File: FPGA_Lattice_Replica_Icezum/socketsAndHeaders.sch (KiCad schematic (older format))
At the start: 38 parts, among them J10 1x8_male_pin_Header_2.54mm, J11 1x6_female_pin_Header_2.54mm, J12 1x6_female_pin_Header_2.54mm, J13 1x6_female_pin_Header_2.54mm, J14 1x6_female_pin_Header_2.54mm, J2 1x6_female_pin_Header_2.54mm, J3 1x6_female_pin_Header_2.54mm, J4 1x10_female_pin_Header_2.54mm, J5 1x8_male_pin_Header_2.54mm, J6 1x6_female_pin_Header_2.54mm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

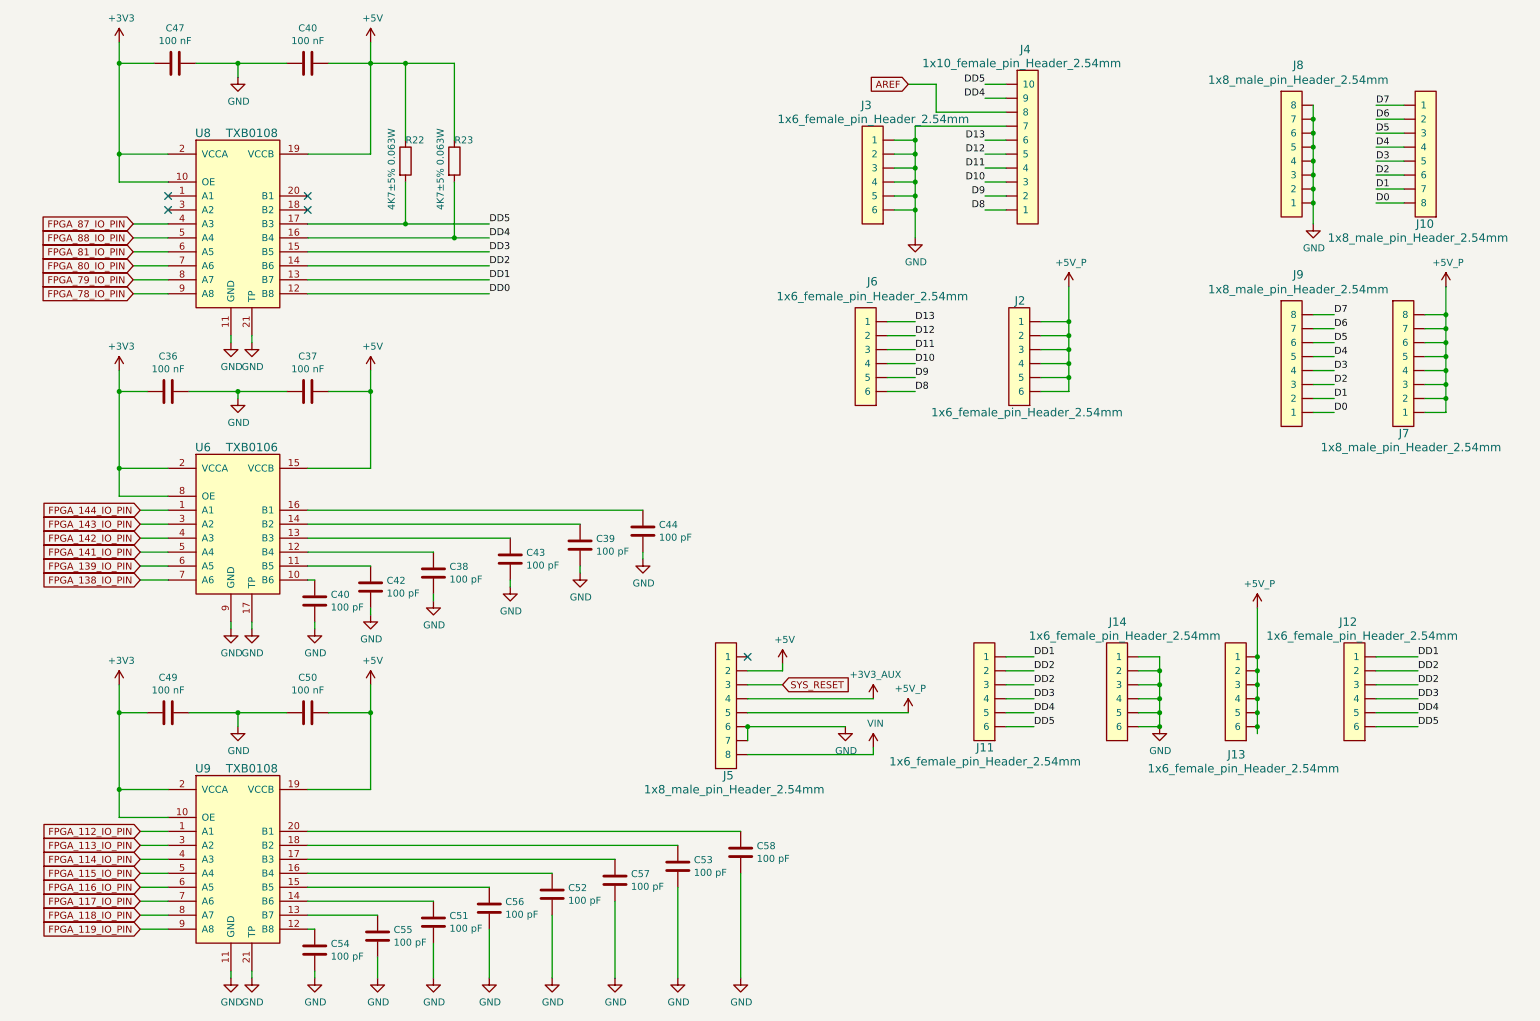
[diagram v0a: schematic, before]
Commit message: se ejecuto y se corrigio electrical rules check
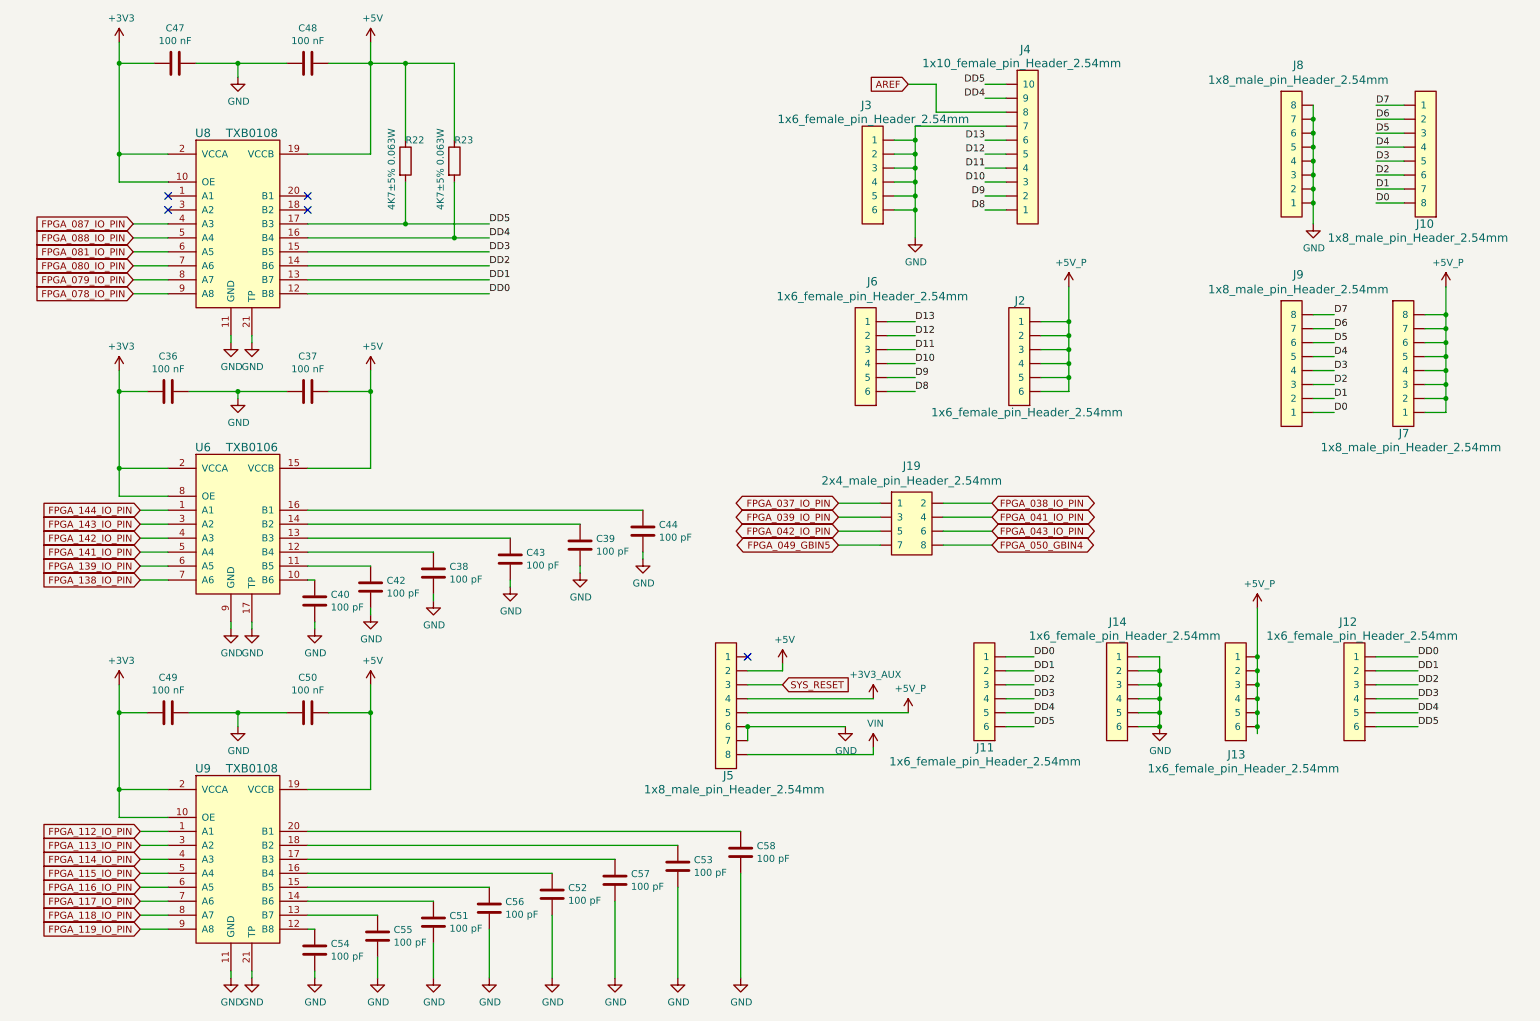
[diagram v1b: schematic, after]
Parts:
- added J19: 2x4_male_pin_Header_2.54mm, symbol icezum:2x4_male_pin_Header_2.54mm
- renumbered C40 to C48
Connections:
- net DD0: now also J11.1, J12.1
- net DD1: now also J11.2, J12.2; no longer J11.1, J12.1
- net DD2: no longer J11.2, J12.2
- net FPGA_78_IO_PIN renamed FPGA_078_IO_PIN
- net FPGA_79_IO_PIN renamed FPGA_079_IO_PIN
- net FPGA_80_IO_PIN renamed FPGA_080_IO_PIN
- net FPGA_81_IO_PIN renamed FPGA_081_IO_PIN
- net FPGA_87_IO_PIN renamed FPGA_087_IO_PIN
- net FPGA_88_IO_PIN renamed FPGA_088_IO_PIN
- new net FPGA_037_IO_PIN: J19.1
- new net FPGA_038_IO_PIN: J19.2
- new net FPGA_039_IO_PIN: J19.3
- new net FPGA_041_IO_PIN: J19.4
- new net FPGA_042_IO_PIN: J19.5
- new net FPGA_043_IO_PIN: J19.6
- new net FPGA_049_GBIN5: J19.7
- new net FPGA_050_GBIN4: J19.8

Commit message: se comenzo asignacion de footprints
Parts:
- C38, C39, C40, C42, C43, C44, C51, C52: footprint (none) -> footprints:C_0402
- C49: footprint (none) -> footprints:C_0603
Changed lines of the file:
@@
 F 0 "U8" H 1850 1650 60  0000 C CNN
 F 1 "TXB0108" H 2200 1650 60  0000 C CNN
-F 2 "" H 2050 1600 60  0000 C CNN
+F 2 "" H 2050 1600 60  0001 C CNN
 F 3 "" H 2050 1600 60  0000 C CNN
 	1    1600 1500
@@
 F 0 "U9" H 1850 6200 60  0000 C CNN
 F 1 "TXB0108" H 2200 6200 60  0000 C CNN
-F 2 "" H 2050 6150 60  0000 C CNN
+F 2 "" H 2050 6150 60  0001 C CNN
 F 3 "" H 2050 6150 60  0000 C CNN
 	1    1600 6050
@@
 F 0 "U6" H 1850 3900 60  0000 C CNN
 F 1 "TXB0106" H 2200 3900 60  0000 C CNN
-F 2 "" H 2050 3850 60  0000 C CNN
+F 2 "" H 2050 3850 60  0001 C CNN
 F 3 "" H 2050 3850 60  0000 C CNN
 	1    1600 3750
@@
 F 0 "C49" V 1348 5500 50  0000 C CNN
 F 1 "100 nF" V 1439 5500 50  0000 C CNN
-F 2 "" H 1638 5350 50  0001 C CNN
+F 2 "footprints:C_0603" H 1638 5350 50  0001 C CNN
 F 3 "~" H 1600 5500 50  0001 C CNN
 	1    1600 5500
@@
 F 0 "C42" H 3165 4646 50  0000 L CNN
 F 1 "100 pF" H 3165 4555 50  0000 L CNN
-F 2 "" H 3088 4450 50  0001 C CNN
+F 2 "footprints:C_0402" H 3088 4450 50  0001 C CNN
 F 3 "~" H 3050 4600 50  0001 C CNN
 	1    3050 4600
@@
 F 0 "C38" H 3615 4546 50  0000 L CNN
 F 1 "100 pF" H 3615 4455 50  0000 L CNN
-F 2 "" H 3538 4350 50  0001 C CNN
+F 2 "footprints:C_0402" H 3538 4350 50  0001 C CNN
 F 3 "~" H 3500 4500 50  0001 C CNN
 	1    3500 4500
@@
 F 0 "C43" H 4165 4446 50  0000 L CNN
 F 1 "100 pF" H 4165 4355 50  0000 L CNN
-F 2 "" H 4088 4250 50  0001 C CNN
+F 2 "footprints:C_0402" H 4088 4250 50  0001 C CNN
 F 3 "~" H 4050 4400 50  0001 C CNN
 	1    4050 4400
@@
 F 0 "C39" H 4665 4346 50  0000 L CNN
 F 1 "100 pF" H 4665 4255 50  0000 L CNN
-F 2 "" H 4588 4150 50  0001 C CNN
+F 2 "footprints:C_0402" H 4588 4150 50  0001 C CNN
 F 3 "~" H 4550 4300 50  0001 C CNN
 	1    4550 4300
@@
 F 0 "C44" H 5115 4246 50  0000 L CNN
 F 1 "100 pF" H 5115 4155 50  0000 L CNN
-F 2 "" H 5038 4050 50  0001 C CNN
+F 2 "footprints:C_0402" H 5038 4050 50  0001 C CNN
 F 3 "~" H 5000 4200 50  0001 C CNN
 	1    5000 4200
@@
 F 0 "C40" H 2765 4746 50  0000 L CNN
 F 1 "100 pF" H 2765 4655 50  0000 L CNN
-F 2 "" H 2688 4550 50  0001 C CNN
+F 2 "footprints:C_0402" H 2688 4550 50  0001 C CNN
 F 3 "~" H 2650 4700 50  0001 C CNN
 	1    2650 4700
@@
 F 0 "C51" H 3615 7046 50  0000 L CNN
 F 1 "100 pF" H 3615 6955 50  0000 L CNN
-F 2 "" H 3538 6850 50  0001 C CNN
+F 2 "footprints:C_0402" H 3538 6850 50  0001 C CNN
 F 3 "~" H 3500 7000 50  0001 C CNN
 	1    3500 7000
@@
 F 0 "C52" H 4465 6846 50  0000 L CNN
 F 1 "100 pF" H 4465 6755 50  0000 L CNN
-F 2 "" H 4388 6650 50  0001 C CNN
+F 2 "footprints:C_0402" H 4388 6650 50  0001 C CNN
 F 3 "~" H 4350 6800 50  0001 C CNN
 	1    4350 6800
@@
 F 0 "J4" H 7700 3050 60  0000 L CNN
 F 1 "1x10_female_pin_Header_2.54mm" H 7000 2950 60  0000 L CNN
-F 2 "" H 7600 2450 60  0000 C CNN
+F 2 "" H 7600 2450 60  0001 C CNN
 F 3 "" H 7600 2450 60  0000 C CNN
 	1    7600 1900
@@
 F 0 "J3" H 7000 1150 60  0000 C CNN
 F 1 "1x6_female_pin_Header_2.54mm" H 6950 1250 60  0000 C CNN
-F 2 "" H 6800 1950 60  0000 C CNN
+F 2 "" H 6800 1950 60  0001 C CNN
 F 3 "" H 6800 1950 60  0000 C CNN
 	1    6800 1400
@@
 F 0 "J6" H 6857 2413 60  0000 C CNN
 F 1 "1x6_female_pin_Header_2.54mm" H 6857 2519 60  0000 C CNN
-F 2 "" H 6750 3250 60  0000 C CNN
+F 2 "" H 6750 3250 60  0001 C CNN
 F 3 "" H 6750 3250 60  0000 C CNN
 	1    6750 2700
@@
 F 0 "J2" H 8000 2550 60  0000 C CNN
 F 1 "1x6_female_pin_Header_2.54mm" H 7950 3350 60  0000 C CNN
-F 2 "" H 7850 3250 60  0000 C CNN
+F 2 "" H 7850 3250 60  0001 C CNN
 F 3 "" H 7850 3250 60  0000 C CNN
 	1    7850 2700
@@
 F 0 "J14" H 8700 4850 60  0000 C CNN
 F 1 "1x6_female_pin_Header_2.54mm" H 8650 4950 60  0000 C CNN
-F 2 "" H 8550 5650 60  0000 C CNN
+F 2 "" H 8550 5650 60  0001 C CNN
 F 3 "" H 8550 5650 60  0000 C CNN
 	1    8550 5100
@@
 F 0 "J13" H 9550 5800 60  0000 C CNN
 F 1 "1x6_female_pin_Header_2.54mm" H 9500 5900 60  0000 C CNN
-F 2 "" H 9400 5650 60  0000 C CNN
+F 2 "" H 9400 5650 60  0001 C CNN
 F 3 "" H 9400 5650 60  0000 C CNN
 	1    9400 5100
@@
 F 0 "J12" H 10450 4850 60  0000 C CNN
 F 1 "1x6_female_pin_Header_2.54mm" H 10350 4950 60  0000 C CNN
-F 2 "" H 10250 5650 60  0000 C CNN
+F 2 "" H 10250 5650 60  0001 C CNN
 F 3 "" H 10250 5650 60  0000 C CNN
 	1    10250 5100
@@
 F 0 "J11" H 7750 5750 60  0000 C CNN
 F 1 "1x6_female_pin_Header_2.54mm" H 7750 5850 60  0000 C CNN
-F 2 "" H 7600 5650 60  0000 C CNN
+F 2 "" H 7600 5650 60  0001 C CNN
 F 3 "" H 7600 5650 60  0000 C CNN
 	1    7600 5100
@@
 F 0 "J7" H 10450 3200 60  0000 C CNN
 F 1 "1x8_male_pin_Header_2.54mm" H 10500 3100 60  0000 C CNN
-F 2 "" H 10600 3900 60  0000 C CNN
+F 2 "" H 10600 3900 60  0001 C CNN
 F 3 "" H 10600 3900 60  0000 C CNN
 	1    10600 3350
@@
 F 0 "J9" H 9693 4337 60  0000 C CNN
 F 1 "1x8_male_pin_Header_2.54mm" H 9693 4231 60  0000 C CNN
-F 2 "" H 9800 3900 60  0000 C CNN
+F 2 "" H 9800 3900 60  0001 C CNN
 F 3 "" H 9800 3900 60  0000 C CNN
 	1    9800 3350
@@
 F 0 "J8" H 9693 2837 60  0000 C CNN
 F 1 "1x8_male_pin_Header_2.54mm" H 9693 2731 60  0000 C CNN
-F 2 "" H 9800 2400 60  0000 C CNN
+F 2 "" H 9800 2400 60  0001 C CNN
 F 3 "" H 9800 2400 60  0000 C CNN
 	1    9800 1850
@@
 F 0 "J10" H 10300 2000 60  0000 C CNN
 F 1 "1x8_male_pin_Header_2.54mm" H 10350 2100 60  0000 C CNN
-F 2 "" H 10450 1700 60  0000 C CNN
+F 2 "" H 10450 1700 60  0001 C CNN
 F 3 "" H 10450 1700 60  0000 C CNN
 	1    10450 1150
@@
 F 0 "J5" H 5650 5950 60  0000 R CNN
 F 1 "1x8_male_pin_Header_2.54mm" H 6300 6050 60  0000 R CNN
-F 2 "" H 5750 5650 60  0000 C CNN
+F 2 "" H 5750 5650 60  0001 C CNN
 F 3 "" H 5750 5650 60  0000 C CNN
 	1    5750 5100
@@
 F 0 "J19" H 6925 4267 60  0000 C CNN
 F 1 "2x4_male_pin_Header_2.54mm" H 6925 4161 60  0000 C CNN
-F 2 "" H 6550 4050 60  0000 C CNN
+F 2 "" H 6550 4050 60  0001 C CNN
 F 3 "" H 6550 4050 60  0000 C CNN
 	1    6700 4000

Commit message: se finalizo asignación de footprint de acuerdo al modelo original de la icezum alhambra
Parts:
- C36, C37, C47, C48, C50, C53, C54, C55, C56, C57, C58: footprint (none) -> footprints:C_0402
- J10, J5, J7, J8, J9: footprint (none) -> footprints:1x8_Socket_header_2.54mm
- J11: footprint (none) -> footprints:1x6-Socket-header-2.54mm
- J12, J13, J14, J2, J3, J6: footprint (none) -> footprints:1x6-pin-header-2.54mm
- J19: footprint (none) -> footprints:2x04-pin-header-2.54mm
- J4: footprint (none) -> footprints:1x10_socket-header-2.54mm
- R22, R23: footprint (none) -> footprints:R_0402
- U6: footprint (none) -> footprints:VQFN16
- U8, U9: footprint (none) -> footprints:VQFN20
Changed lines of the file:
@@
 F 0 "U8" H 1850 1650 60  0000 C CNN
 F 1 "TXB0108" H 2200 1650 60  0000 C CNN
-F 2 "" H 2050 1600 60  0001 C CNN
+F 2 "footprints:VQFN20" H 2050 1600 60  0001 C CNN
 F 3 "" H 2050 1600 60  0000 C CNN
 	1    1600 1500
@@
 F 0 "U9" H 1850 6200 60  0000 C CNN
 F 1 "TXB0108" H 2200 6200 60  0000 C CNN
-F 2 "" H 2050 6150 60  0001 C CNN
+F 2 "footprints:VQFN20" H 2050 6150 60  0001 C CNN
 F 3 "" H 2050 6150 60  0000 C CNN
 	1    1600 6050
@@
 F 0 "U6" H 1850 3900 60  0000 C CNN
 F 1 "TXB0106" H 2200 3900 60  0000 C CNN
-F 2 "" H 2050 3850 60  0001 C CNN
+F 2 "footprints:VQFN16" H 2050 3850 60  0001 C CNN
 F 3 "" H 2050 3850 60  0000 C CNN
 	1    1600 3750
@@
 F 0 "C47" V 1398 850 50  0000 C CNN
 F 1 "100 nF" V 1489 850 50  0000 C CNN
-F 2 "" H 1688 700 50  0001 C CNN
+F 2 "footprints:C_0402" H 1688 700 50  0001 C CNN
 F 3 "~" H 1650 850 50  0001 C CNN
 	1    1650 850
@@
 F 0 "C48" V 2348 850 50  0000 C CNN
 F 1 "100 nF" V 2439 850 50  0000 C CNN
-F 2 "" H 2638 700 50  0001 C CNN
+F 2 "footprints:C_0402" H 2638 700 50  0001 C CNN
 F 3 "~" H 2600 850 50  0001 C CNN
 	1    2600 850
@@
 F 0 "C37" V 2348 3200 50  0000 C CNN
 F 1 "100 nF" V 2439 3200 50  0000 C CNN
-F 2 "" H 2638 3050 50  0001 C CNN
+F 2 "footprints:C_0402" H 2638 3050 50  0001 C CNN
 F 3 "~" H 2600 3200 50  0001 C CNN
 	1    2600 3200
@@
 F 0 "C36" V 1348 3200 50  0000 C CNN
 F 1 "100 nF" V 1439 3200 50  0000 C CNN
-F 2 "" H 1638 3050 50  0001 C CNN
+F 2 "footprints:C_0402" H 1638 3050 50  0001 C CNN
 F 3 "~" H 1600 3200 50  0001 C CNN
 	1    1600 3200
@@
 F 0 "C50" V 2348 5500 50  0000 C CNN
 F 1 "100 nF" V 2439 5500 50  0000 C CNN
-F 2 "" H 2638 5350 50  0001 C CNN
+F 2 "footprints:C_0402" H 2638 5350 50  0001 C CNN
 F 3 "~" H 2600 5500 50  0001 C CNN
 	1    2600 5500
@@
 F 0 "C54" H 2765 7246 50  0000 L CNN
 F 1 "100 pF" H 2765 7155 50  0000 L CNN
-F 2 "" H 2688 7050 50  0001 C CNN
+F 2 "footprints:C_0402" H 2688 7050 50  0001 C CNN
 F 3 "~" H 2650 7200 50  0001 C CNN
 	1    2650 7200
@@
 F 0 "C55" H 3215 7146 50  0000 L CNN
 F 1 "100 pF" H 3215 7055 50  0000 L CNN
-F 2 "" H 3138 6950 50  0001 C CNN
+F 2 "footprints:C_0402" H 3138 6950 50  0001 C CNN
 F 3 "~" H 3100 7100 50  0001 C CNN
 	1    3100 7100
@@
 F 0 "C56" H 4015 6946 50  0000 L CNN
 F 1 "100 pF" H 4015 6855 50  0000 L CNN
-F 2 "" H 3938 6750 50  0001 C CNN
+F 2 "footprints:C_0402" H 3938 6750 50  0001 C CNN
 F 3 "~" H 3900 6900 50  0001 C CNN
 	1    3900 6900
@@
 F 0 "C57" H 4915 6746 50  0000 L CNN
 F 1 "100 pF" H 4915 6655 50  0000 L CNN
-F 2 "" H 4838 6550 50  0001 C CNN
+F 2 "footprints:C_0402" H 4838 6550 50  0001 C CNN
 F 3 "~" H 4800 6700 50  0001 C CNN
 	1    4800 6700
@@
 F 0 "C53" H 5365 6646 50  0000 L CNN
 F 1 "100 pF" H 5365 6555 50  0000 L CNN
-F 2 "" H 5288 6450 50  0001 C CNN
+F 2 "footprints:C_0402" H 5288 6450 50  0001 C CNN
 F 3 "~" H 5250 6600 50  0001 C CNN
 	1    5250 6600
@@
 F 0 "C58" H 5815 6546 50  0000 L CNN
 F 1 "100 pF" H 5815 6455 50  0000 L CNN
-F 2 "" H 5738 6350 50  0001 C CNN
+F 2 "footprints:C_0402" H 5738 6350 50  0001 C CNN
 F 3 "~" H 5700 6500 50  0001 C CNN
 	1    5700 6500
@@
 F 0 "R22" H 3300 1700 50  0000 L CNN
 F 1 "4K7±5% 0.063W" V 3200 1200 50  0000 L CNN
-F 2 "" V 3230 1550 50  0001 C CNN
+F 2 "footprints:R_0402" V 3230 1550 50  0001 C CNN
 F 3 "~" H 3300 1550 50  0001 C CNN
 	1    3300 1550
@@
 F 0 "R23" H 3650 1700 50  0000 L CNN
 F 1 "4K7±5% 0.063W" V 3550 1200 50  0000 L CNN
-F 2 "" V 3580 1550 50  0001 C CNN
+F 2 "footprints:R_0402" V 3580 1550 50  0001 C CNN
 F 3 "~" H 3650 1550 50  0001 C CNN
 	1    3650 1550
@@
 F 0 "J4" H 7700 3050 60  0000 L CNN
 F 1 "1x10_female_pin_Header_2.54mm" H 7000 2950 60  0000 L CNN
-F 2 "" H 7600 2450 60  0001 C CNN
+F 2 "footprints:1x10_socket-header-2.54mm" H 7600 2450 60  0001 C CNN
 F 3 "" H 7600 2450 60  0000 C CNN
 	1    7600 1900
@@
 F 0 "J3" H 7000 1150 60  0000 C CNN
 F 1 "1x6_female_pin_Header_2.54mm" H 6950 1250 60  0000 C CNN
-F 2 "" H 6800 1950 60  0001 C CNN
+F 2 "footprints:1x6-pin-header-2.54mm" H 6800 1950 60  0001 C CNN
 F 3 "" H 6800 1950 60  0000 C CNN
 	1    6800 1400
@@
 F 0 "J6" H 6857 2413 60  0000 C CNN
 F 1 "1x6_female_pin_Header_2.54mm" H 6857 2519 60  0000 C CNN
-F 2 "" H 6750 3250 60  0001 C CNN
+F 2 "footprints:1x6-pin-header-2.54mm" H 6750 3250 60  0001 C CNN
 F 3 "" H 6750 3250 60  0000 C CNN
 	1    6750 2700
@@
 F 0 "J2" H 8000 2550 60  0000 C CNN
 F 1 "1x6_female_pin_Header_2.54mm" H 7950 3350 60  0000 C CNN
-F 2 "" H 7850 3250 60  0001 C CNN
+F 2 "footprints:1x6-pin-header-2.54mm" H 7850 3250 60  0001 C CNN
 F 3 "" H 7850 3250 60  0000 C CNN
 	1    7850 2700
@@
 F 0 "J14" H 8700 4850 60  0000 C CNN
 F 1 "1x6_female_pin_Header_2.54mm" H 8650 4950 60  0000 C CNN
-F 2 "" H 8550 5650 60  0001 C CNN
+F 2 "footprints:1x6-pin-header-2.54mm" H 8550 5650 60  0001 C CNN
 F 3 "" H 8550 5650 60  0000 C CNN
 	1    8550 5100
@@
 F 0 "J13" H 9550 5800 60  0000 C CNN
 F 1 "1x6_female_pin_Header_2.54mm" H 9500 5900 60  0000 C CNN
-F 2 "" H 9400 5650 60  0001 C CNN
+F 2 "footprints:1x6-pin-header-2.54mm" H 9400 5650 60  0001 C CNN
 F 3 "" H 9400 5650 60  0000 C CNN
 	1    9400 5100
@@
 F 0 "J12" H 10450 4850 60  0000 C CNN
 F 1 "1x6_female_pin_Header_2.54mm" H 10350 4950 60  0000 C CNN
-F 2 "" H 10250 5650 60  0001 C CNN
+F 2 "footprints:1x6-pin-header-2.54mm" H 10250 5650 60  0001 C CNN
 F 3 "" H 10250 5650 60  0000 C CNN
 	1    10250 5100
@@
 F 0 "J11" H 7750 5750 60  0000 C CNN
 F 1 "1x6_female_pin_Header_2.54mm" H 7750 5850 60  0000 C CNN
-F 2 "" H 7600 5650 60  0001 C CNN
+F 2 "footprints:1x6-Socket-header-2.54mm" H 7600 5650 60  0001 C CNN
 F 3 "" H 7600 5650 60  0000 C CNN
 	1    7600 5100
@@
 F 0 "J7" H 10450 3200 60  0000 C CNN
 F 1 "1x8_male_pin_Header_2.54mm" H 10500 3100 60  0000 C CNN
-F 2 "" H 10600 3900 60  0001 C CNN
+F 2 "footprints:1x8_Socket_header_2.54mm" H 10600 3900 60  0001 C CNN
 F 3 "" H 10600 3900 60  0000 C CNN
 	1    10600 3350
@@
 F 0 "J9" H 9693 4337 60  0000 C CNN
 F 1 "1x8_male_pin_Header_2.54mm" H 9693 4231 60  0000 C CNN
-F 2 "" H 9800 3900 60  0001 C CNN
+F 2 "footprints:1x8_Socket_header_2.54mm" H 9800 3900 60  0001 C CNN
 F 3 "" H 9800 3900 60  0000 C CNN
 	1    9800 3350
@@
 F 0 "J8" H 9693 2837 60  0000 C CNN
 F 1 "1x8_male_pin_Header_2.54mm" H 9693 2731 60  0000 C CNN
-F 2 "" H 9800 2400 60  0001 C CNN
+F 2 "footprints:1x8_Socket_header_2.54mm" H 9800 2400 60  0001 C CNN
 F 3 "" H 9800 2400 60  0000 C CNN
 	1    9800 1850
@@
 F 0 "J10" H 10300 2000 60  0000 C CNN
 F 1 "1x8_male_pin_Header_2.54mm" H 10350 2100 60  0000 C CNN
-F 2 "" H 10450 1700 60  0001 C CNN
+F 2 "footprints:1x8_Socket_header_2.54mm" H 10450 1700 60  0001 C CNN
 F 3 "" H 10450 1700 60  0000 C CNN
 	1    10450 1150
@@
 F 0 "J5" H 5650 5950 60  0000 R CNN
 F 1 "1x8_male_pin_Header_2.54mm" H 6300 6050 60  0000 R CNN
-F 2 "" H 5750 5650 60  0001 C CNN
+F 2 "footprints:1x8_Socket_header_2.54mm" H 5750 5650 60  0001 C CNN
 F 3 "" H 5750 5650 60  0000 C CNN
 	1    5750 5100
@@
 F 0 "J19" H 6925 4267 60  0000 C CNN
 F 1 "2x4_male_pin_Header_2.54mm" H 6925 4161 60  0000 C CNN
-F 2 "" H 6550 4050 60  0001 C CNN
+F 2 "footprints:2x04-pin-header-2.54mm" H 6550 4050 60  0001 C CNN
 F 3 "" H 6550 4050 60  0000 C CNN
 	1    6700 4000

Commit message: se coloco hojas de datos de los componentes
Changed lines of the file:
@@
 F 1 "TXB0108" H 2200 1650 60  0000 C CNN
 F 2 "footprints:VQFN20" H 2050 1600 60  0001 C CNN
-F 3 "" H 2050 1600 60  0000 C CNN
+F 3 "txs0108e.pdf" H 2550 350 60  0000 C CNN
 	1    1600 1500
 	1    0    0    -1
@@
 F 1 "TXB0108" H 2200 6200 60  0000 C CNN
 F 2 "footprints:VQFN20" H 2050 6150 60  0001 C CNN
-F 3 "" H 2050 6150 60  0000 C CNN
+F 3 "txb0108.pdf" H 1700 4900 60  0000 C CNN
 	1    1600 6050
 	1    0    0    -1
@@
 F 1 "TXB0106" H 2200 3900 60  0000 C CNN
 F 2 "footprints:VQFN16" H 2050 3850 60  0001 C CNN
-F 3 "" H 2050 3850 60  0000 C CNN
+F 3 "txb0106.pdf" H 1650 2750 60  0000 C CNN
 	1    1600 3750
 	1    0    0    -1
